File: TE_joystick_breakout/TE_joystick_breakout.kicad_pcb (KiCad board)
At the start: 2 copper layers, 18.5 x 18.8 mm, 12 parts, among them J1 2434804-1, J2 Conn_01x04, J3 Conn_01x04, SW1 SW_Push

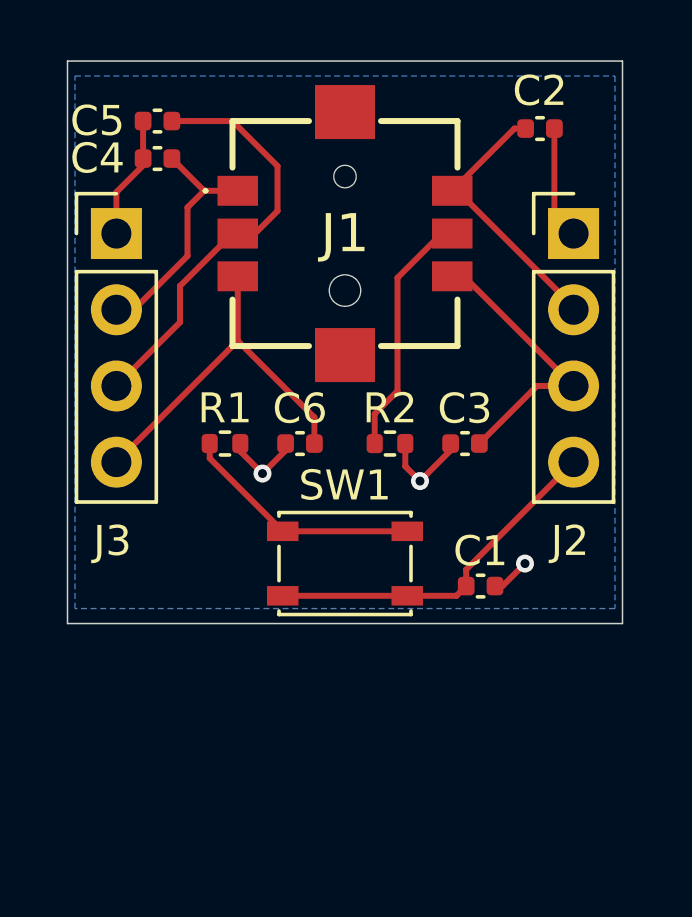
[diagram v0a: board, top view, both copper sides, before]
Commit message: Redesign joystick breakout
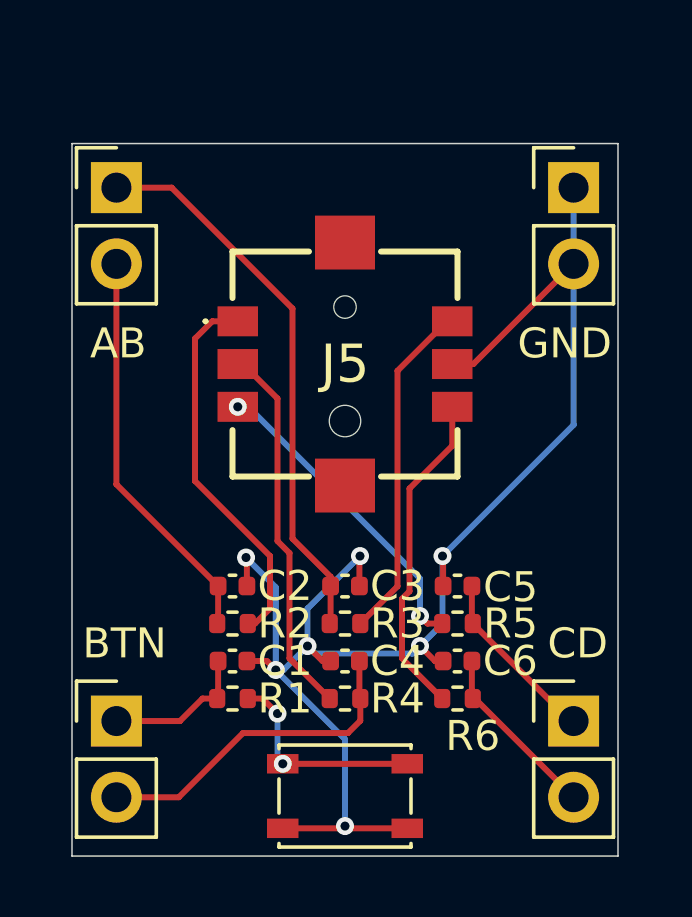
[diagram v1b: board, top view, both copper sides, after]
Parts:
- removed the C6 at (148.5, 107.0)
- added C2: 470n, Capacitor_SMD:C_0402_1005Metric, F.Cu at (146.2, 111.8)
- added J1: Conn_01x02, Connector_PinHeader_2.54mm:PinHeader_1x02_P2.54mm_Vertical, F.Cu at (157.6, 98.5)
- added J4: Conn_01x02, Connector_PinHeader_2.54mm:PinHeader_1x02_P2.54mm_Vertical, F.Cu at (157.6, 116.2)
- added R3: 10K, Resistor_SMD:R_0402_1005Metric, F.Cu at (150.0, 113.0)
- added R4: 10K, Resistor_SMD:R_0402_1005Metric, F.Cu at (150.0, 115.5)
- added R5: 10K, Resistor_SMD:R_0402_1005Metric, F.Cu at (153.8, 113.0)
- added R6: 10K, Resistor_SMD:R_0402_1005Metric, F.Cu at (153.8, 115.5)
- C1, C4, C5: value C -> 470n
- C3: renamed from C2; value C -> 470n
- C6: renamed from C3; value C -> 470n
- J2, J3: value Conn_01x04 -> Conn_01x02; footprint Connector_PinHeader_2.54mm:PinHeader_1x04_P2.54mm_Vertical -> Connector_PinHeader_2.54mm:PinHeader_1x02_P2.54mm_Vertical
- R1, R2: value R -> 10K
- moved J2 22.3 mm to (142.4, 116.2)
- moved C5 18.4 mm to (153.8, 111.8), turned to 180 degrees
- moved C4 17.9 mm to (150.0, 114.2), turned to 0 degrees
- moved C3 16.6 mm to (150.0, 111.8)
- moved C1 8.64 mm to (146.2, 114.2)
- moved R1 8.50 mm to (146.2, 115.5), turned to 180 degrees
- moved R2 7.97 mm to (146.2, 113.0), turned to 180 degrees
- moved SW1 7.75 mm to (150.0, 118.8), turned to 180 degrees
- moved C6 7.25 mm to (153.8, 114.2), turned to 180 degrees
- moved J5 4.35 mm to (150.0, 104.3)
- moved J3 1.53 mm to (142.4, 98.5)
- renumbered J1 to J5
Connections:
- C1 pad 1: Net-(J2-Pin_4) -> /BUTTON
- C3 pad 2: Net-(J1-B) -> /DIR_B
- C4 pad 1: Net-(J1-A) -> GND
- C4 pad 2: GND -> /CENTER
- C5 pad 1: GND -> /DIR_C
- C5 pad 2: Net-(J1-CENTER) -> GND
- C6 pad 1: GND -> /DIR_D
- C6 pad 2: Net-(J1-D) -> GND
- J2 pad 1: GND -> /BUTTON
- J2 pad 2: Net-(J1-B) -> /CENTER
- J3 pad 1: GND -> /DIR_B
- J3 pad 2: Net-(J1-A) -> /DIR_A
- J5 pad 1: Net-(J1-A) -> Net-(J5-A)
- J5 pad 2: Net-(J1-CENTER) -> Net-(J5-CENTER)
- J5 pad 3: Net-(J1-C) -> Net-(J5-C)
- J5 pad 4: Net-(J1-B) -> Net-(J5-B)
- J5 pad 5: Net-(J1-C/M) -> GND
- J5 pad 6: Net-(J1-D) -> Net-(J5-D)
- R1 pad 2: GND -> /BUTTON
- R2 pad 1: Net-(J1-C/M) -> Net-(J5-A)
- R2 pad 2: GND -> /DIR_A
- SW1 pad 1: Net-(R1-Pad1) -> GND
- SW1 pad 2: Net-(J2-Pin_4) -> Net-(R1-Pad1)
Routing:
- net GND: track 14.9 -> 52.4 mm, vias 3 -> 7
- net /DIR_B: track 0.00 -> 18.5 mm
- net Net-(J1-CENTER): track 14.1 -> 0.00 mm
- net /DIR_A: track 0.00 -> 13.4 mm
- net Net-(J5-A): track 0.00 -> 12.6 mm
- net Net-(J1-C): track 12.4 -> 0.00 mm
- net Net-(J5-CENTER): track 0.00 -> 12.3 mm
- net Net-(J2-Pin_4): track 11.9 -> 0.00 mm
- net Net-(J5-B): track 0.00 -> 11.3 mm
- net /CENTER: track 0.00 -> 11.1 mm
- net Net-(J5-D): track 0.00 -> 11.0 mm
- net Net-(J5-C): track 0.00 -> 10.5 mm, vias 0 -> 2
- net Net-(J1-D): track 9.49 -> 0.00 mm
- net Net-(J1-B): track 9.05 -> 0.00 mm
- net Net-(J1-C/M): track 8.28 -> 0.00 mm
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- removed copper zone on B.Cu, net GND
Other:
- board size 18.5 x 18.8 mm -> 18.2 x 23.8 mm
- board text added: "AB"
- board text added: "BTN"
- board text added: "CD"
- board text added: "GND"

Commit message: Rotate joystick 45 degrees to get proper axis directions
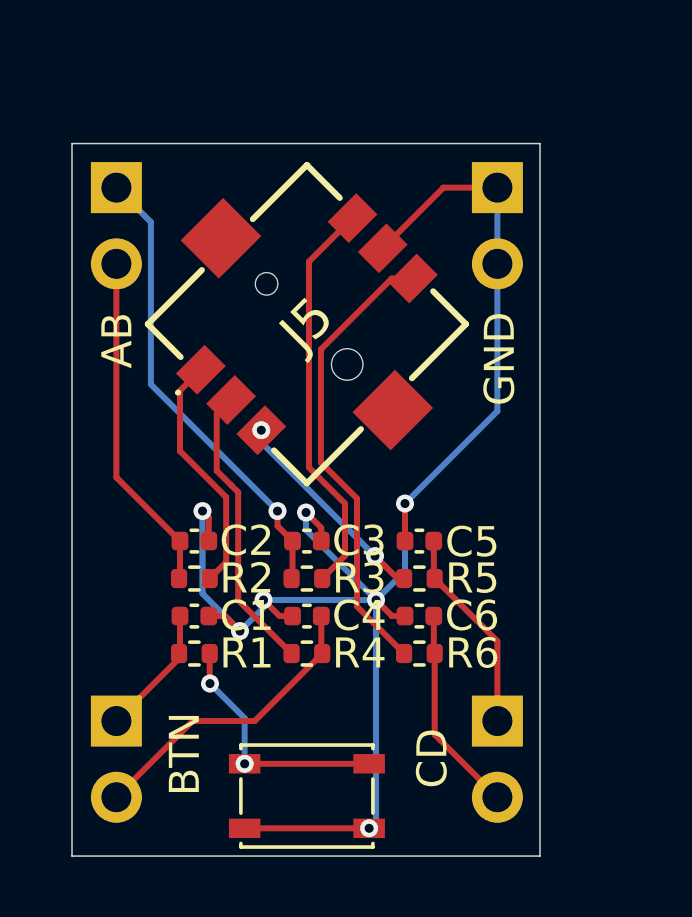
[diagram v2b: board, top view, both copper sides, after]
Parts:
- J1, J2, J3, J4: moved to B.Cu
- moved J1 2.54 mm to (155.1, 98.5), turned to 180 degrees
- moved J4 2.54 mm to (155.1, 116.2), turned to 180 degrees
- moved C1 1.97 mm to (145.0, 112.8)
- moved C2 1.97 mm to (145.0, 110.2)
- moved C3 1.97 mm to (148.7, 110.2)
- moved C4 1.97 mm to (148.7, 112.8)
- moved C5 1.97 mm to (152.5, 110.2)
- moved C6 1.97 mm to (152.5, 112.8)
- moved R1 1.97 mm to (145.0, 114.0)
- moved R2 1.97 mm to (145.0, 111.5)
- moved R3 1.97 mm to (148.7, 111.5)
- moved R4 1.97 mm to (148.7, 114.0)
- moved R5 1.97 mm to (152.5, 111.5)
- moved R6 1.97 mm to (152.5, 114.0)
- moved J5 1.84 mm to (148.7, 103.0), turned to 45 degrees
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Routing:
- net Net-(J5-A): track 12.6 -> 8.11 mm
- net Net-(J5-D): track 11.0 -> 15.3 mm
- net Net-(J5-C): track 10.5 -> 7.04 mm
- net /DIR_B: track 18.5 -> 15.4 mm, vias 0 -> 1
- net Net-(J5-CENTER): track 12.3 -> 9.68 mm
- net Net-(J5-B): track 11.3 -> 13.4 mm
- net /DIR_A: track 13.4 -> 11.4 mm
- net Net-(R1-Pad1): track 7.09 -> 8.31 mm
- net /CENTER: track 11.1 -> 10.1 mm
- net /DIR_D: track 5.87 -> 6.92 mm
- net /DIR_C: track 5.82 -> 6.84 mm
- net /BUTTON: track 4.89 -> 4.34 mm
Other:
- board size 18.2 x 23.8 mm -> 15.6 x 23.8 mm
